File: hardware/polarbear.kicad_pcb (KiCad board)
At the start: 2 copper layers, 182.6 x 100 mm, 85 parts, among them IC1 ATMEGA32U4, J1 USBMICRO, X1 ATS16B

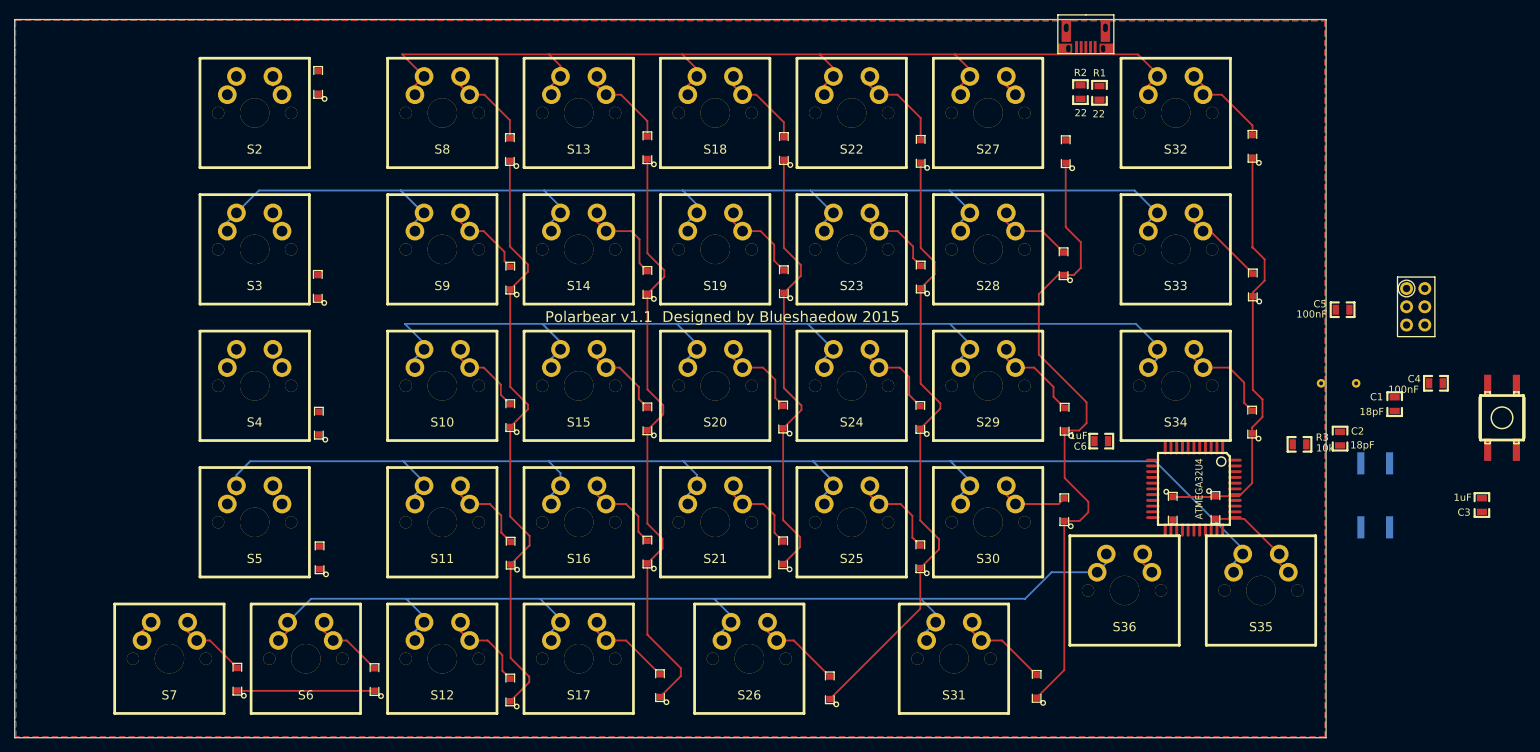
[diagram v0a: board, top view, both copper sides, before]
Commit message: Adding support for Tennsy 2.0
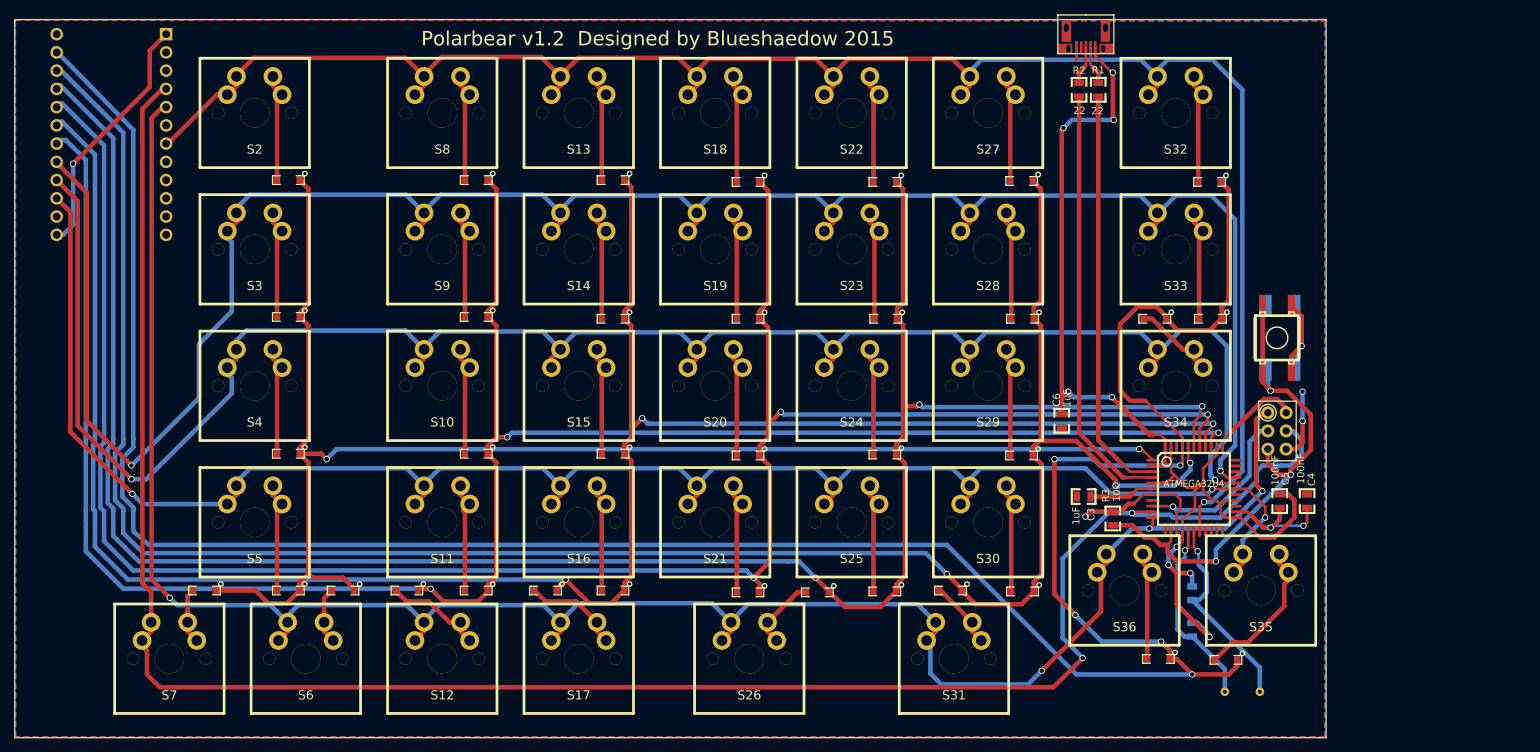
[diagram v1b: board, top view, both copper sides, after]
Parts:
- added U1: TEENSY2.0, lib_kicad_mod:TEENSY_2.0, B.Cu at (66.5, 46.0)
- C1, C2: moved to B.Cu
- moved C3 55.5 mm to (201.8, 96.4), turned to 180 degrees
- moved X1 45.0 mm to (223.9, 123.6)
- moved C1 42.2 mm to (217.0, 115.0), turned to 90 degrees
- moved S1 33.2 mm to (228.8, 74.3)
- moved C2 29.8 mm to (217.0, 109.9), turned to 90 degrees
- moved C5 28.1 mm to (229.1, 97.1), turned to 90 degrees
- moved R3 28.0 mm to (205.9, 99.5), turned to 270 degrees
- moved H1 25.9 mm to (230.0, 84.7)
- moved S1 25.5 mm to (229.5, 74.3), turned to 90 degrees
- moved C4 24.3 mm to (233.0, 97.1), turned to 90 degrees
- moved D34 21.3 mm to (221.7, 119.2), turned to 180 degrees
- moved D35 21.1 mm to (212.3, 119.0), turned to 180 degrees
- moved D16 20.7 mm to (126.9, 109.5), turned to 180 degrees
- moved D11 20.0 mm to (107.6, 109.5), turned to 180 degrees
- moved D33 19.8 mm to (211.8, 71.7), turned to 180 degrees
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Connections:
- net Net-(D10-Pad1) renamed /PF7
- net Net-(D12-Pad1) renamed /PF6
- net Net-(D17-Pad1) renamed /PF5
- net Net-(D21-Pad1) renamed /PF4
- net Net-(D26-Pad1) renamed /PF1
- net Net-(D31-Pad1) renamed /PF0
- net Net-(IC1-Pad28) renamed /PB4
- net Net-(IC1-Pad29) renamed /PB5
- net Net-(IC1-Pad30) renamed /PB6
- D1 pad 1: Net-(D1-Pad1) -> /PE6
- D2 pad 1: Net-(D1-Pad1) -> /PE6
- D3 pad 1: Net-(D1-Pad1) -> /PE6
- D4 pad 1: Net-(D1-Pad1) -> /PE6
- D5 pad 1: Net-(D1-Pad1) -> /PE6
- D6 pad 1: Net-(D1-Pad1) -> /PE6
- IC1 pad 1: (no net) -> /PE6
- IC1 pad 12: (no net) -> Net-(IC1-Pad12)
- IC1 pad 18: (no net) -> /PD0
- IC1 pad 19: (no net) -> Net-(IC1-Pad19)
- IC1 pad 20: (no net) -> Net-(IC1-Pad20)
- IC1 pad 21: (no net) -> Net-(IC1-Pad21)
- IC1 pad 22: (no net) -> Net-(IC1-Pad22)
- IC1 pad 25: (no net) -> Net-(IC1-Pad25)
- IC1 pad 26: (no net) -> GND
- IC1 pad 27: (no net) -> Net-(IC1-Pad27)
- IC1 pad 31: (no net) -> Net-(IC1-Pad31)
- IC1 pad 32: Net-(D1-Pad1) -> Net-(IC1-Pad32)
- IC1 pad 42: (no net) -> Net-(IC1-Pad42)
- IC1 pad 8: (no net) -> Net-(IC1-Pad8)
- J1 pad 4: (no net) -> Net-(J1-Pad4)
- S13 pad 1: Net-(IC1-Pad33) -> /PD0
- S18 pad 1: Net-(IC1-Pad33) -> /PD0
- S2 pad 1: Net-(IC1-Pad33) -> /PD0
- S22 pad 1: Net-(IC1-Pad33) -> /PD0
- S27 pad 1: Net-(IC1-Pad33) -> /PD0
- S32 pad 1: Net-(IC1-Pad33) -> /PD0
- S8 pad 1: Net-(IC1-Pad33) -> /PD0
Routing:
- net /PF0: track 60.0 -> 359.7 mm, vias 0 -> 5
- net /MOSI: track 3.07 -> 281.1 mm, vias 0 -> 2
- net /PD0: track 0.00 -> 255.8 mm, vias 0 -> 1
- net /PF5: track 62.3 -> 288.6 mm, vias 0 -> 3
- net /PF6: track 83.5 -> 288.3 mm, vias 0 -> 3
- net /PF4: track 86.0 -> 289.0 mm, vias 0 -> 3
- net /PF7: track 83.7 -> 284.9 mm, vias 0 -> 3
- net /PE6: track 0.00 -> 201.2 mm, vias 0 -> 2
- net /PF1: track 89.8 -> 289.7 mm, vias 0 -> 3
- net Net-(IC1-Pad33): track 146.4 -> 0.00 mm
- net GND: track 0.00 -> 136.2 mm, vias 0 -> 8
- net /MISO: track 151.5 -> 285.7 mm, vias 0 -> 4
- net VCC: track 0.00 -> 132.8 mm, vias 0 -> 8
- net /PB6: track 175.8 -> 301.1 mm, vias 0 -> 2
- net /PB5: track 152.2 -> 266.2 mm, vias 0 -> 2
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- added copper zone on B.Cu, net VCC
- removed copper zone on B.Cu, net (none)
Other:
- board text added: "Polarbear v1.2 Designed by Blueshaedow 2015"
- board text removed: "Polarbear v1.1 Designed by Blueshaedow 2015"

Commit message: Adding WS2128 LED module
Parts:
- added LED1: WS2812, lib_kicad_mod:WS2128, F.Cu at (228.8, 43.0)
- added LED1: WS2812, lib_kicad_mod:WS2128, F.Cu at (60.4, 115.7)
- S10, S11, S12, S13, S14, S15, S16, S17, S18, S19, S2, S20, S21, S22, S23, S24, S25, S26, S27, S28, S29, S3, S30, S31, S32, S33, S34, S35, S36, S4, S5, S6, S7, S8, S9: footprint lib_kicad_mod:MX1A_ddouble_sided -> lib_kicad_mod:MX1A_ddouble_sided_big_ring
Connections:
- IC1 pad 8: Net-(IC1-Pad8) -> /PB0
- S1 pad 2: (no net) -> GND
- S1 pad 4: (no net) -> /RESb
- U1 pad 2: Net-(U1-Pad2) -> /PB0
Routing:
- net /PB0: track 0.00 -> 437.1 mm, vias 0 -> 5
- net VCC: track 132.8 -> 163.4 mm, vias 8 -> 5
- net GND: track 136.2 -> 150.0 mm
- net /RESb: track 73.7 -> 82.6 mm
- net /PD0: track 255.8 -> 251.0 mm
- net /PB6: track 301.1 -> 303.8 mm
- net /RD+: track 59.7 -> 62.3 mm
- net /PF1: track 289.7 -> 287.3 mm
- net /RD-: track 57.2 -> 59.0 mm
- net /PF7: track 284.9 -> 286.3 mm
- net /PF6: track 288.3 -> 289.5 mm
- net /PF5: track 288.6 -> 289.7 mm
- net /PF4: track 289.0 -> 289.9 mm
- net /PF0: track 359.7 -> 360.4 mm
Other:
- board text added: "Left hand dominant"
- board text added: "Polarbear v1.2 Designed by Blueshaedow July 2016"
- board text removed: "Polarbear v1.2 Designed by Blueshaedow 2015"

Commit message: Modified design to include 3 WS2128 LED module, added open hardware logo, and re-did routing for VDD/GND.
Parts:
- removed the LED1 at (228.8, 43.0)
- added LED2: WS2812, lib_kicad_mod:WS2128, F.Cu at (229.1, 41.6)
- added LED3: WS2812, lib_kicad_mod:WS2128, F.Cu at (229.1, 57.6)
- added open_hardware_logo: , lib_kicad_mod:open_hardware_logo, F.Cu at (93.6, 79.5)
- moved C6 41.9 mm to (198.5, 44.0), turned to 90 degrees
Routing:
- net GND: track 150.0 -> 217.9 mm, vias 8 -> 10
- net VCC: track 163.4 -> 149.4 mm, vias 5 -> 8
- net /PF0: track 360.4 -> 354.4 mm, vias 5 -> 4
- net Net-(LED2-Pad5): track 0.00 -> 5.84 mm
- net /PB0: track 437.1 -> 439.4 mm
- net /PD0: track 251.0 -> 252.5 mm
- net /PB6: track 303.8 -> 302.5 mm
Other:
- board text added: "Left hand dominant Designed on Kicad"
- board text removed: "Left hand dominant"
